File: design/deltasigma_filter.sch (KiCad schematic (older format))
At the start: 13 parts, among them U2 OPA376AID, U4 Buffer

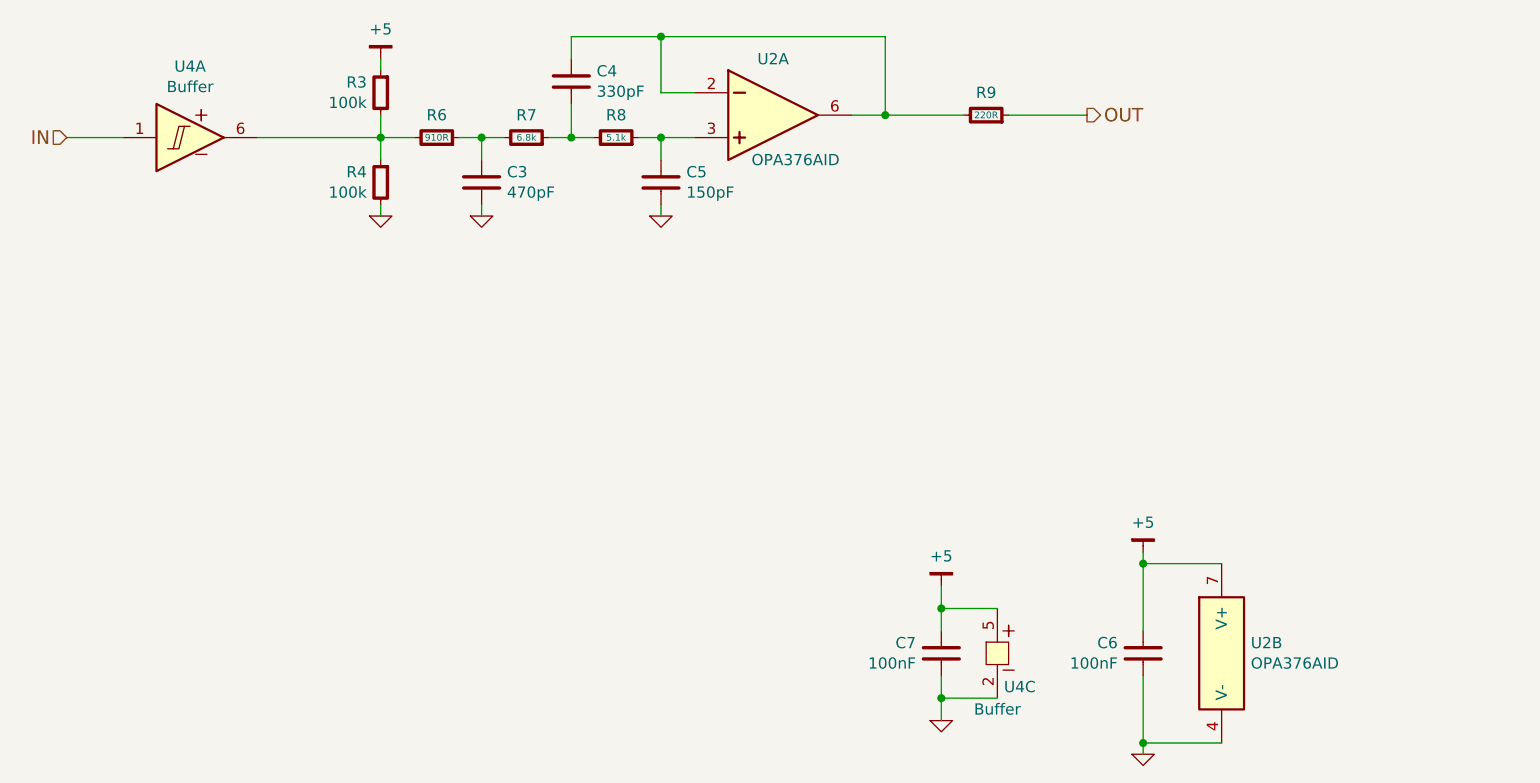
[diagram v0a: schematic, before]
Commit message: Added buffer to restore signal before opamp analog filter
Signed-off-by: Marcos Chaparro <mchaparro@paltatech.com>
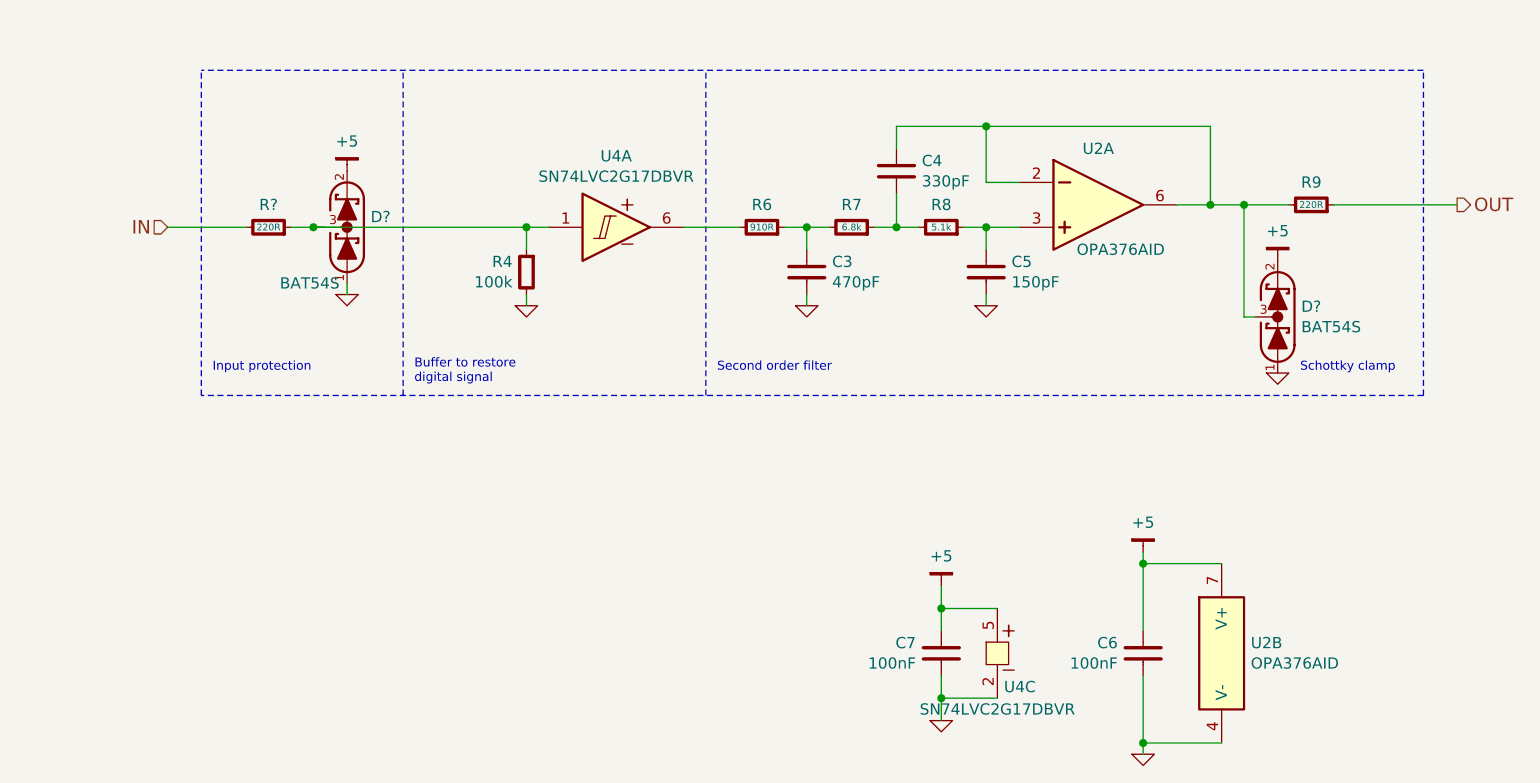
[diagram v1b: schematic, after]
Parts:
- removed R3: 100k, IPC7351-Nominal:RESC1608X50, symbol R-0603
- added D? (x2): BAT54S, smd-semi:SOT-23, symbol BAT54S
- added R?: 220R, IPC7351-Nominal:RESC1608X50, symbol R-0603
- U4: value Buffer -> SN74LVC2G17DBVR
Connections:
- net +5: now also D?.2 (K), D?.2 (K)
- net GND: now also D?.1 (A), D?.1 (A)
- net IN: now also R?.2; no longer U4.1 (1A)
- net at C4.1, R9.2, U2.2 (IN-)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: now also D?.3 (COM)
- net at R6.2, U4.6 (1Y): no longer R4.1
- new net: D?.3 (COM), R4.1, R?.1, U4.1 (1A)
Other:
- note added: "Buffer to restore\ndigital signal"
- note added: "Input protection"
- note added: "Schottky clamp"
- note added: "Second order filter"
- moved on the sheet: C3, C4, C5, R4, R6, R7, R8, R9, U2A, U4A

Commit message: Added harness fault protections
Signed-off-by: Marcos Chaparro <mchaparro@paltatech.com>
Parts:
- gave numbers to parts that had none: 3
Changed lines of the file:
@@
 $EndComp
 Wire Wire Line
-	7400 3450 7550 3450
-Wire Wire Line
-	7550 3450 7700 3450
-Wire Wire Line
-	7700 3450 7900 3450
+	7400 3450 7900 3450
 Wire Wire Line
 	7550 3100 7550 3450
 Wire Wire Line
-	6150 3100 6550 3100
-Wire Wire Line
-	6550 3100 7550 3100
+	6150 3100 7550 3100
 Wire Wire Line
 	6550 3100 6550 3350
@@
 $EndComp
 Wire Wire Line
-	6050 3550 6150 3550
-Wire Wire Line
-	6150 3550 6250 3550
+	6050 3550 6250 3550
 Wire Wire Line
 	6150 3550 6150 3400
 Connection ~ 6150 3550
 Wire Wire Line
-	5650 3550 5750 3550
-Wire Wire Line
-	5750 3550 5850 3550
+	5650 3550 5850 3550
 Wire Wire Line
 	5750 3550 5750 3650
@@
 Connection ~ 6550 3100
 Wire Wire Line
-	6450 3550 6550 3550
-Wire Wire Line
-	6550 3550 6700 3550
+	6450 3550 6700 3550
 Wire Wire Line
 	6550 3550 6550 3650
@@
 $EndComp
 Wire Wire Line
-	7250 5000 7250 5050
-Wire Wire Line
-	7250 5050 7250 5350
+	7250 5000 7250 5350
 Wire Wire Line
 	7250 5050 7600 5050
 Wire Wire Line
-	7250 5550 7250 5850
-Wire Wire Line
-	7250 5850 7250 5900
+	7250 5550 7250 5900
 Wire Wire Line
 	7250 5850 7600 5850
@@
 $EndComp
 Wire Wire Line
-	3450 3550 3550 3550
-Wire Wire Line
-	3550 3550 4500 3550
-Wire Wire Line
-	4500 3550 4600 3550
+	3450 3550 4600 3550
 $Comp
 L BUF-Schmitt-Dual U?
@@
 	6600 5250 6350 5250
 Wire Wire Line
-	6350 5150 6350 5250
-Wire Wire Line
-	6350 5250 6350 5350
+	6350 5150 6350 5350
 Wire Wire Line
 	6600 5650 6350 5650
 Wire Wire Line
-	6350 5550 6350 5650
-Wire Wire Line
-	6350 5650 6350 5750
+	6350 5550 6350 5750
 $Comp
 L GND #PWR?
@@
 	3050 4300 3050 2850
 $Comp
-L BAT54S D?
+L BAT54S D2
 U 1 1 59971BC7
 P 7850 3950
-F 0 "D?" V 7896 3845 50  0000 R CNN
+F 0 "D2" V 7896 3845 50  0000 R CNN
 F 1 "BAT54S" V 7805 3845 50  0000 R CNN
 F 2 "smd-semi:SOT-23" H 7850 3800 60  0001 C CNN
@@
 P 7850 3700
 AR Path="/59971D1A" Ref="#PWR?"  Part="1"
-AR Path="/59903B4B/59971D1A" Ref="#PWR?"  Part="1"
-F 0 "#PWR?" H 7850 3750 30  0001 C CNN
+AR Path="/59903B4B/59971D1A" Ref="#PWR019"  Part="1"
+F 0 "#PWR019" H 7850 3750 30  0001 C CNN
 F 1 "+5" H 7850 3833 50  0000 C CNN
 F 2 "" H 7850 3700 60  0000 C CNN
@@
 P 7850 4200
 AR Path="/59971D9D" Ref="#PWR?"  Part="1"
-AR Path="/59903B4B/59971D9D" Ref="#PWR?"  Part="1"
-F 0 "#PWR?" H 7850 4200 30  0001 C CNN
+AR Path="/59903B4B/59971D9D" Ref="#PWR025"  Part="1"
+F 0 "#PWR025" H 7850 4200 30  0001 C CNN
 F 1 "GND" H 7850 4130 30  0001 C CNN
 F 2 "" H 7850 4200 60  0000 C CNN
@@
 Schottky clamp
 $Comp
-L BAT54S D?
+L BAT54S D1
 U 1 1 59971F51
 P 3700 3550
-F 0 "D?" V 3746 3445 50  0000 R CNN
+F 0 "D1" V 3746 3445 50  0000 R CNN
 F 1 "BAT54S" V 3450 3850 50  0000 R CNN
 F 2 "smd-semi:SOT-23" H 3700 3400 60  0001 C CNN
@@
 	3550 3550 3600 3550
 $Comp
-L GND #PWR?
+L GND #PWR026
 U 1 1 59972098
 P 3700 3850
-F 0 "#PWR?" H 3700 3850 30  0001 C CNN
+F 0 "#PWR026" H 3700 3850 30  0001 C CNN
 F 1 "GND" H 3700 3780 30  0001 C CNN
 F 2 "" H 3700 3850 60  0000 C CNN
@@
 P 3700 3300
 AR Path="/59972135" Ref="#PWR?"  Part="1"
-AR Path="/59903B4B/59972135" Ref="#PWR?"  Part="1"
-F 0 "#PWR?" H 3700 3350 30  0001 C CNN
+AR Path="/59903B4B/59972135" Ref="#PWR027"  Part="1"
+F 0 "#PWR027" H 3700 3350 30  0001 C CNN
 F 1 "+5" H 3700 3433 50  0000 C CNN
 F 2 "" H 3700 3300 60  0000 C CNN
@@
 $EndComp
 $Comp
-L R-0603 R?
+L R-0603 R11
 U 1 1 599722AD
 P 3350 3550
-F 0 "R?" V 3450 3550 50  0000 C CNN
+F 0 "R11" V 3450 3550 50  0000 C CNN
 F 1 "220R" V 3350 3550 30  0000 C CNN
 F 2 "IPC7351-Nominal:RESC1608X50" H 3350 3550 50  0001 C CNN
